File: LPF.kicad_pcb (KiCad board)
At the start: 2 copper layers, 100 x 100 mm, 109 parts, among them P1 SMA, P2 J5/J5' Ctrl Brd, P3 SMA, U1 7805D-Pack

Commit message: version 1.1
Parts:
- removed C69: CP, Capacitors_SMD:C_0805_HandSoldering
- removed R2: OR, Resistors_SMD:R_0805_HandSoldering
- removed U1: 7805D-Pack, TO_SOT_Packages_SMD:TO-252-3_TabPin4
- added P4: SMA, SMA_PINS:SMA_PINS, F.Cu at (73.0, 142.9)
-  : renamed from TP1; value TEST -> (none)
-  : renamed from TP2; value TEST -> (none)
-  : renamed from TP3; value TEST -> (none)
-  : renamed from TP4; value TEST -> (none)
- C67: value CP -> 10n
- C68: value CP -> 100n
- RL1, RL10, RL11, RL12, RL13, RL14, RL2, RL3, RL4, RL5, RL6, RL7, RL8, RL9: value EE2-5NU -> EC2-12NU
- moved L14 151.3 mm to (120.0, 116.8)
- moved RL7 135.7 mm to (76.0, 128.0), turned to 270 degrees
- moved L15 125.5 mm to (120.0, 129.5)
- moved RL5 115.7 mm to (76.0, 102.0), turned to 270 degrees
- moved L8 115.4 mm to (105.4, 129.5)
- moved RL6 114.3 mm to (76.0, 115.0), turned to 270 degrees
- moved RL15 102.5 mm to (88.9, 141.6), turned to 90 degrees
- moved RL3 102.0 mm to (76.0, 76.0), turned to 270 degrees
- moved RL4 101.8 mm to (76.0, 89.0), turned to 270 degrees
- moved L2 98.9 mm to (90.2, 129.5)
- moved L7 96.3 mm to (90.2, 116.2)
- moved C5 93.8 mm to (187.0, 31.0)
- moved RL8 93.2 mm to (134.0, 50.0), turned to 90 degrees
- moved C3 90.9 mm to (187.0, 35.0)
- moved C4 90.5 mm to (182.0, 31.0)
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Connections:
- net 12/10 renamed 12/10m
- net 160 renamed 160m
- net 17/15 renamed 17/15m
- net 30/20 renamed 30/20m
- net 6/Bypass renamed 6m_Bypass
- net 60/40 renamed 40m
- C1 pad 1: +5V -> +12V
- C2 pad 1: +5V -> +12V
- C3 pad 1: +5V -> +12V
- C4 pad 1: +5V -> +12V
- C5 pad 1: +5V -> +12V
- C6 pad 1: +5V -> +12V
- C60 pad 1: +5V -> +12V
- C61 pad 1: +5V -> +12V
- C62 pad 1: +5V -> +12V
- C63 pad 1: +5V -> +12V
- C64 pad 1: +5V -> +12V
- C65 pad 1: +5V -> +12V
- C66 pad 1: +5V -> +12V
- C7 pad 1: +5V -> +12V
- P2 pad 8: GND -> TX_RX_RLY
- RL1 pad 1: +5V -> +12V
- RL1 pad 5: Net-(P1-Pad1) -> Net-(RL1-Pad5)
- RL1 pad 8: Net-(P1-Pad1) -> Net-(RL1-Pad5)
- RL10 pad 1: +5V -> +12V
- RL10 pad 5: Net-(FL1-Pad6) -> Net-(P3-Pad1)
- RL10 pad 8: Net-(FL1-Pad6) -> Net-(P3-Pad1)
- RL11 pad 1: +5V -> +12V
- RL11 pad 5: Net-(FL1-Pad6) -> Net-(P3-Pad1)
- RL11 pad 8: Net-(FL1-Pad6) -> Net-(P3-Pad1)
- RL12 pad 1: +5V -> +12V
- RL12 pad 5: Net-(FL1-Pad6) -> Net-(P3-Pad1)
- RL12 pad 8: Net-(FL1-Pad6) -> Net-(P3-Pad1)
- RL13 pad 1: +5V -> +12V
- RL13 pad 5: Net-(FL1-Pad6) -> Net-(P3-Pad1)
- RL13 pad 8: Net-(FL1-Pad6) -> Net-(P3-Pad1)
- RL14 pad 1: +5V -> +12V
- RL14 pad 5: Net-(FL1-Pad6) -> Net-(P3-Pad1)
- RL14 pad 8: Net-(FL1-Pad6) -> Net-(P3-Pad1)
- RL15 pad 1: +5V -> +12V
- RL15 pad 12: (no net) -> TX_RX_RLY
- RL15 pad 4: Net-(P3-Pad1) -> Net-(RL1-Pad5)
- RL15 pad 5: GND -> Net-(P1-Pad1)
- RL15 pad 8: GND -> Net-(P1-Pad1)
- RL15 pad 9: Net-(P3-Pad1) -> Net-(RL1-Pad5)
- RL2 pad 1: +5V -> +12V
- RL2 pad 5: Net-(P1-Pad1) -> Net-(RL1-Pad5)
- RL2 pad 8: Net-(P1-Pad1) -> Net-(RL1-Pad5)
- RL3 pad 1: +5V -> +12V
- RL3 pad 5: Net-(P1-Pad1) -> Net-(RL1-Pad5)
- RL3 pad 8: Net-(P1-Pad1) -> Net-(RL1-Pad5)
- RL4 pad 1: +5V -> +12V
- RL4 pad 5: Net-(P1-Pad1) -> Net-(RL1-Pad5)
- RL4 pad 8: Net-(P1-Pad1) -> Net-(RL1-Pad5)
- RL5 pad 1: +5V -> +12V
- RL5 pad 5: Net-(P1-Pad1) -> Net-(RL1-Pad5)
- RL5 pad 8: Net-(P1-Pad1) -> Net-(RL1-Pad5)
- RL6 pad 1: +5V -> +12V
- RL6 pad 5: Net-(P1-Pad1) -> Net-(RL1-Pad5)
- RL6 pad 8: Net-(P1-Pad1) -> Net-(RL1-Pad5)
- RL7 pad 1: +5V -> +12V
- RL7 pad 5: Net-(P1-Pad1) -> Net-(RL1-Pad5)
- RL7 pad 8: Net-(P1-Pad1) -> Net-(RL1-Pad5)
- RL8 pad 1: +5V -> +12V
- RL8 pad 5: Net-(FL1-Pad6) -> Net-(P3-Pad1)
- RL8 pad 8: Net-(FL1-Pad6) -> Net-(P3-Pad1)
- RL9 pad 1: +5V -> +12V
- RL9 pad 5: Net-(FL1-Pad6) -> Net-(P3-Pad1)
- RL9 pad 8: Net-(FL1-Pad6) -> Net-(P3-Pad1)
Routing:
- net +12V: track 0.00 -> 544.2 mm, vias 0 -> 8
- net Net-(RL1-Pad5): track 0.00 -> 114.9 mm
- net Net-(P3-Pad1): track 0.00 -> 96.2 mm
- net 6m_Bypass: track 0.00 -> 75.6 mm
- net TX_RX_RLY: track 0.00 -> 54.6 mm
- net 160m: track 0.00 -> 47.5 mm
- net 12/10m: track 0.00 -> 42.3 mm
- net 80m: track 0.00 -> 39.3 mm
- net Net-(C21-Pad2): track 0.00 -> 36.1 mm
- net Net-(C19-Pad2): track 0.00 -> 35.8 mm
- net Net-(C20-Pad2): track 0.00 -> 35.8 mm
- net Net-(C22-Pad2): track 0.00 -> 35.6 mm
- net Net-(C44-Pad2): track 0.00 -> 34.9 mm
- net Net-(C43-Pad2): track 0.00 -> 34.5 mm
- net Net-(C39-Pad2): track 0.00 -> 34.3 mm
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
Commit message: minor changes, adding kk lib, still under dev.
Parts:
- moved C19 20.0 mm to (84.0, 48.0), turned to 270 degrees
- moved C20 20.0 mm to (84.0, 60.0), turned to 270 degrees
- moved C46 18.3 mm to (126.0, 55.0), turned to 90 degrees
- moved C47 18.3 mm to (126.0, 67.0), turned to 90 degrees
- moved C32 7.07 mm to (100.5, 53.0), turned to 90 degrees
- moved C33 5.35 mm to (111.0, 60.5), turned to 270 degrees
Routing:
- net 17/15m: track 31.5 -> 81.4 mm
- net 40m: track 28.9 -> 78.9 mm
- net 80m: track 39.3 -> 89.3 mm
- net 30/20m: track 25.1 -> 75.0 mm
- net 12/10m: track 42.3 -> 92.3 mm
- net 160m: track 47.5 -> 97.4 mm
- net 6m_Bypass: track 75.6 -> 102.4 mm
- net +12V: track 544.2 -> 546.0 mm
- net Net-(C39-Pad2): track 34.3 -> 35.9 mm
- net Net-(C20-Pad2): track 35.8 -> 37.4 mm
- net Net-(C22-Pad2): track 35.6 -> 36.6 mm
- net Net-(C21-Pad2): track 36.1 -> 37.1 mm
- net Net-(C25-Pad2): track 26.9 -> 26.1 mm
- net Net-(C26-Pad2): track 27.8 -> 27.1 mm
- net Net-(C40-Pad2): track 34.2 -> 34.8 mm

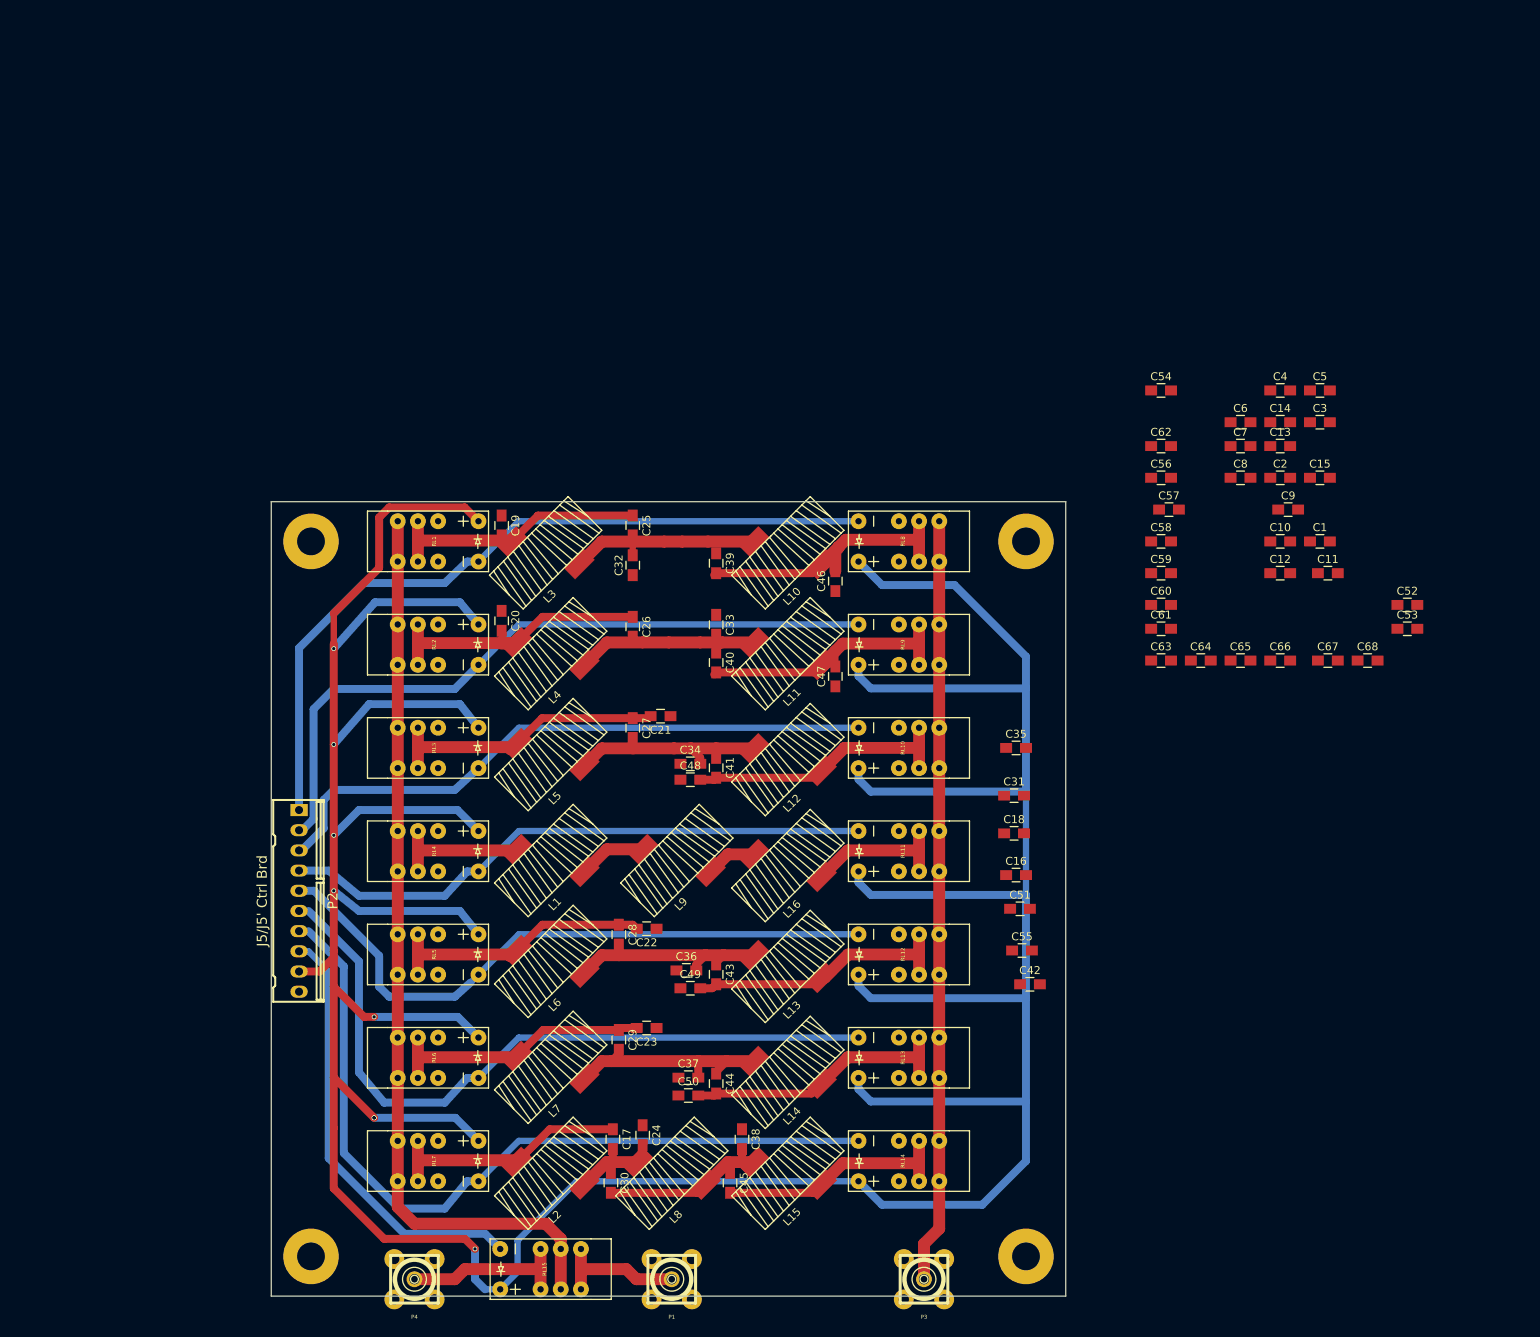
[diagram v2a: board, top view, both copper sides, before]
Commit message: new 4 layers routing, mods in schematic
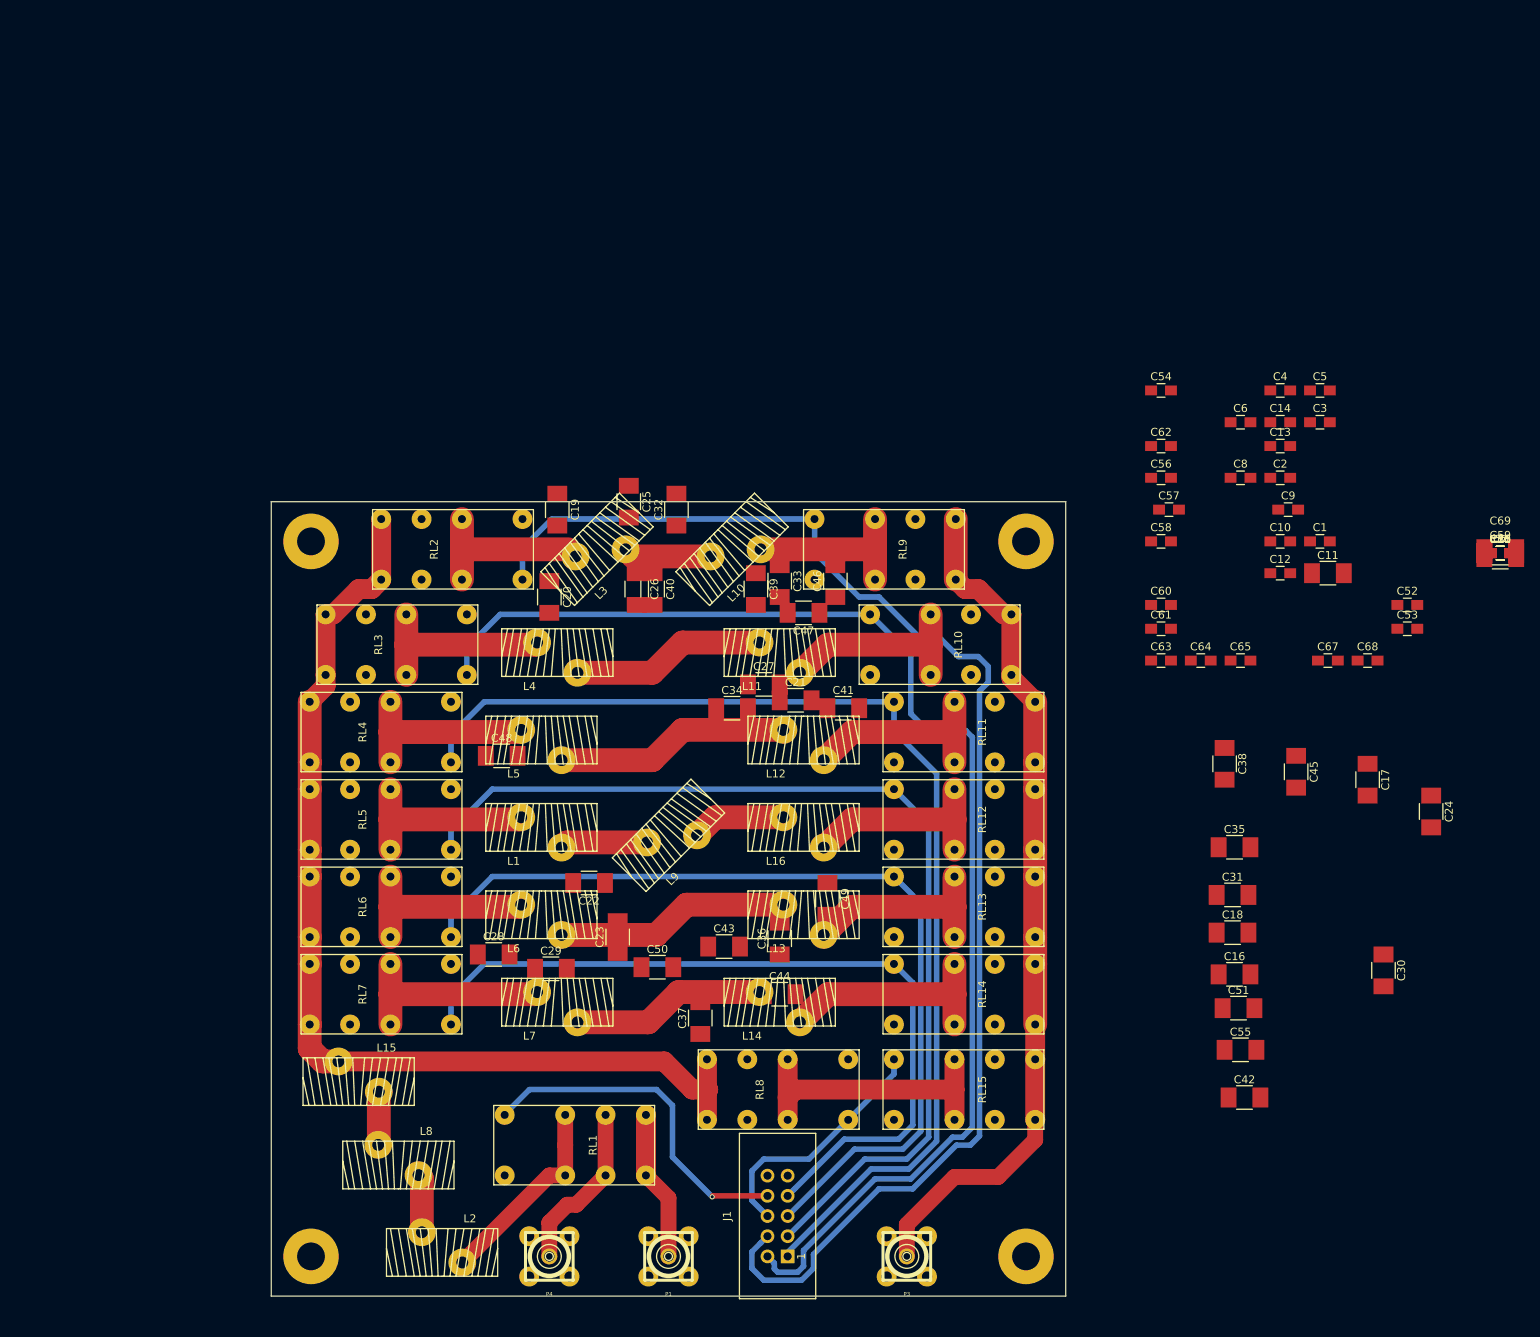
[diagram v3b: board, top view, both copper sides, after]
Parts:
- removed P2: J5/J5' Ctrl Brd, conn_kk100:kk100_22-23-2101
- added C69: C, ATC_B:ATC_500_HandSoldering, F.Cu at (209.7, 51.5)
- added C70, C71: 10n, Capacitors_SMD:C_0805_HandSoldering, F.Cu at (209.7, 51.5)
- added J1: Conn_02x05_Counter_Clockwise, Connectors:IDC_Header_Straight_10pins, F.Cu at (120.0, 140.0)
- C11, C16, C18, C19, C20, C21, C22, C23, C25, C26, C27, C28, C29, C31, C32, C33, C34, C35, C36, C37, C39, C40, C41, C42, C43, C44, C46, C47, C48, C49, C50, C51, C55: footprint Capacitors_SMD:C_0805_HandSoldering -> Capacitors_SMD:C_1210_HandSoldering
- C17: value C -> 24p; footprint Capacitors_SMD:C_0805_HandSoldering -> Capacitors_SMD:C_1210_HandSoldering
- C24: value C -> 31p; footprint Capacitors_SMD:C_0805_HandSoldering -> Capacitors_SMD:C_1210_HandSoldering
- C30: value C -> 15p; footprint Capacitors_SMD:C_0805_HandSoldering -> Capacitors_SMD:C_1210_HandSoldering
- C38: value C -> 68p; footprint Capacitors_SMD:C_0805_HandSoldering -> Capacitors_SMD:C_1210_HandSoldering
- C45: value C -> 4.7; footprint Capacitors_SMD:C_0805_HandSoldering -> Capacitors_SMD:C_1210_HandSoldering
- C59: value 10n -> 24p; footprint Capacitors_SMD:C_0805_HandSoldering -> Capacitors_SMD:C_1210_HandSoldering
- L1, L10, L11, L12, L13, L14, L15, L16, L2, L3, L4, L5, L6, L7, L8, L9: footprint T50_V_cms:T50_V_smd -> T50:T50_V_THT
- RL1, RL10, RL11, RL12, RL13, RL14, RL2, RL3, RL4, RL5, RL6, RL7, RL8, RL9: value EC2-12NU -> D2n; footprint 2_Form_C_Relay:THT_2_formC -> 2_Form_C_Relay:D2n
- RL15: value EE2-5NU -> D2n; footprint 2_Form_C_Relay:THT_2_formC -> 2_Form_C_Relay:D2n
- TP1, TP2, TP3, TP4: renamed from  ; value (none) -> TEST
- moved C24 107.3 mm to (201.0, 84.0)
- moved C17 105.2 mm to (193.0, 80.0)
- moved C30 100.9 mm to (195.0, 104.0)
- moved C45 88.1 mm to (184.0, 79.0)
- moved RL1 77.7 mm to (92.0, 126.0), turned to 90 degrees
- moved C38 77.0 mm to (175.0, 78.0)
- moved RL8 70.4 mm to (120.0, 119.0), turned to 270 degrees
- moved RL15 56.8 mm to (141.0, 119.0)
- moved L15 55.2 mm to (66.0, 118.0), turned to 180 degrees
- moved C59 42.8 mm to (209.7, 51.5)
- moved C7 35.4 mm to (209.7, 51.5)
- moved L8 34.4 mm to (71.0, 128.5), turned to 180 degrees
- moved C66 30.8 mm to (209.7, 51.5)
- moved C42 30.5 mm to (177.5, 120.0)
- moved C16 30.2 mm to (176.2, 104.5)
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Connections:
- C15 pad 1: 6m_Bypass -> +12V
- C59 pad 1: GND -> Net-(C45-Pad2)
- C59 pad 2: 6m_Bypass -> GND
- C66 pad 1: +12V -> 6m_Bypass
- C7 pad 1: +12V -> TX_RX_RLY
- RL1 pad 4: Net-(C19-Pad2) -> Net-(C17-Pad1)
- RL1 pad 8: Net-(RL1-Pad5) -> Net-(P1-Pad1)
- RL1 pad 9: Net-(C19-Pad2) -> Net-(P1-Pad1)
- RL10 pad 4: Net-(C41-Pad2) -> Net-(C40-Pad2)
- RL10 pad 9: Net-(C41-Pad2) -> Net-(P3-Pad1)
- RL11 pad 4: Net-(C51-Pad2) -> Net-(C41-Pad2)
- RL11 pad 9: Net-(C51-Pad2) -> Net-(P3-Pad1)
- RL12 pad 4: Net-(C43-Pad2) -> Net-(C51-Pad2)
- RL12 pad 9: Net-(C43-Pad2) -> Net-(P3-Pad1)
- RL13 pad 4: Net-(C44-Pad2) -> Net-(C43-Pad2)
- RL13 pad 9: Net-(C44-Pad2) -> Net-(P3-Pad1)
- RL14 pad 4: Net-(C45-Pad2) -> Net-(C44-Pad2)
- RL14 pad 9: Net-(C45-Pad2) -> Net-(P3-Pad1)
- RL15 pad 4: Net-(RL1-Pad5) -> Net-(C69-Pad1)
- RL15 pad 8: Net-(P1-Pad1) -> Net-(P3-Pad1)
- RL15 pad 9: Net-(RL1-Pad5) -> Net-(P3-Pad1)
- RL2 pad 4: Net-(C20-Pad2) -> Net-(C19-Pad2)
- RL2 pad 8: Net-(RL1-Pad5) -> Net-(C45-Pad2)
- RL2 pad 9: Net-(C20-Pad2) -> Net-(C45-Pad2)
- RL3 pad 4: Net-(C21-Pad2) -> Net-(C20-Pad2)
- RL3 pad 8: Net-(RL1-Pad5) -> Net-(C45-Pad2)
- RL3 pad 9: Net-(C21-Pad2) -> Net-(C45-Pad2)
- RL4 pad 4: Net-(C11-Pad2) -> Net-(C21-Pad2)
- RL4 pad 8: Net-(RL1-Pad5) -> Net-(C45-Pad2)
- RL4 pad 9: Net-(C11-Pad2) -> Net-(C45-Pad2)
- RL5 pad 4: Net-(C22-Pad2) -> Net-(C11-Pad2)
- RL5 pad 8: Net-(RL1-Pad5) -> Net-(C45-Pad2)
- RL5 pad 9: Net-(C22-Pad2) -> Net-(C45-Pad2)
- RL6 pad 4: Net-(C23-Pad2) -> Net-(C22-Pad2)
- RL6 pad 8: Net-(RL1-Pad5) -> Net-(C45-Pad2)
- RL6 pad 9: Net-(C23-Pad2) -> Net-(C45-Pad2)
- RL7 pad 4: Net-(C17-Pad1) -> Net-(C23-Pad2)
- RL7 pad 8: Net-(RL1-Pad5) -> Net-(C45-Pad2)
- RL7 pad 9: Net-(C17-Pad1) -> Net-(C45-Pad2)
- RL8 pad 4: Net-(C39-Pad2) -> Net-(C69-Pad1)
- RL8 pad 8: Net-(P3-Pad1) -> Net-(C45-Pad2)
- RL8 pad 9: Net-(C39-Pad2) -> Net-(C45-Pad2)
- RL9 pad 4: Net-(C40-Pad2) -> Net-(C39-Pad2)
- RL9 pad 9: Net-(C40-Pad2) -> Net-(P3-Pad1)
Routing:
- net +12V: track 546.0 -> 4.43 mm, vias 8 -> 0
- net Net-(RL1-Pad5): track 114.9 -> 0.00 mm
- net Net-(C45-Pad2): track 30.4 -> 132.0 mm
- net 160m: track 97.4 -> 177.2 mm
- net 80m: track 89.3 -> 164.4 mm
- net 6m_Bypass: track 102.4 -> 31.3 mm
- net 40m: track 78.9 -> 143.5 mm
- net 30/20m: track 75.0 -> 129.9 mm
- net Net-(C69-Pad1): track 0.00 -> 36.7 mm
- net 17/15m: track 81.4 -> 115.0 mm
- net Net-(C30-Pad2): track 22.9 -> 6.72 mm
- net Net-(C25-Pad2): track 26.1 -> 11.1 mm
- net Net-(C39-Pad2): track 35.9 -> 22.0 mm
- net Net-(C20-Pad2): track 37.4 -> 24.2 mm
- net Net-(C19-Pad2): track 35.3 -> 22.3 mm
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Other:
- copper layers 2 -> 4
